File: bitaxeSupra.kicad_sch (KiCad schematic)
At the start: 20 parts, among them J1 PJ-036AH-SMT

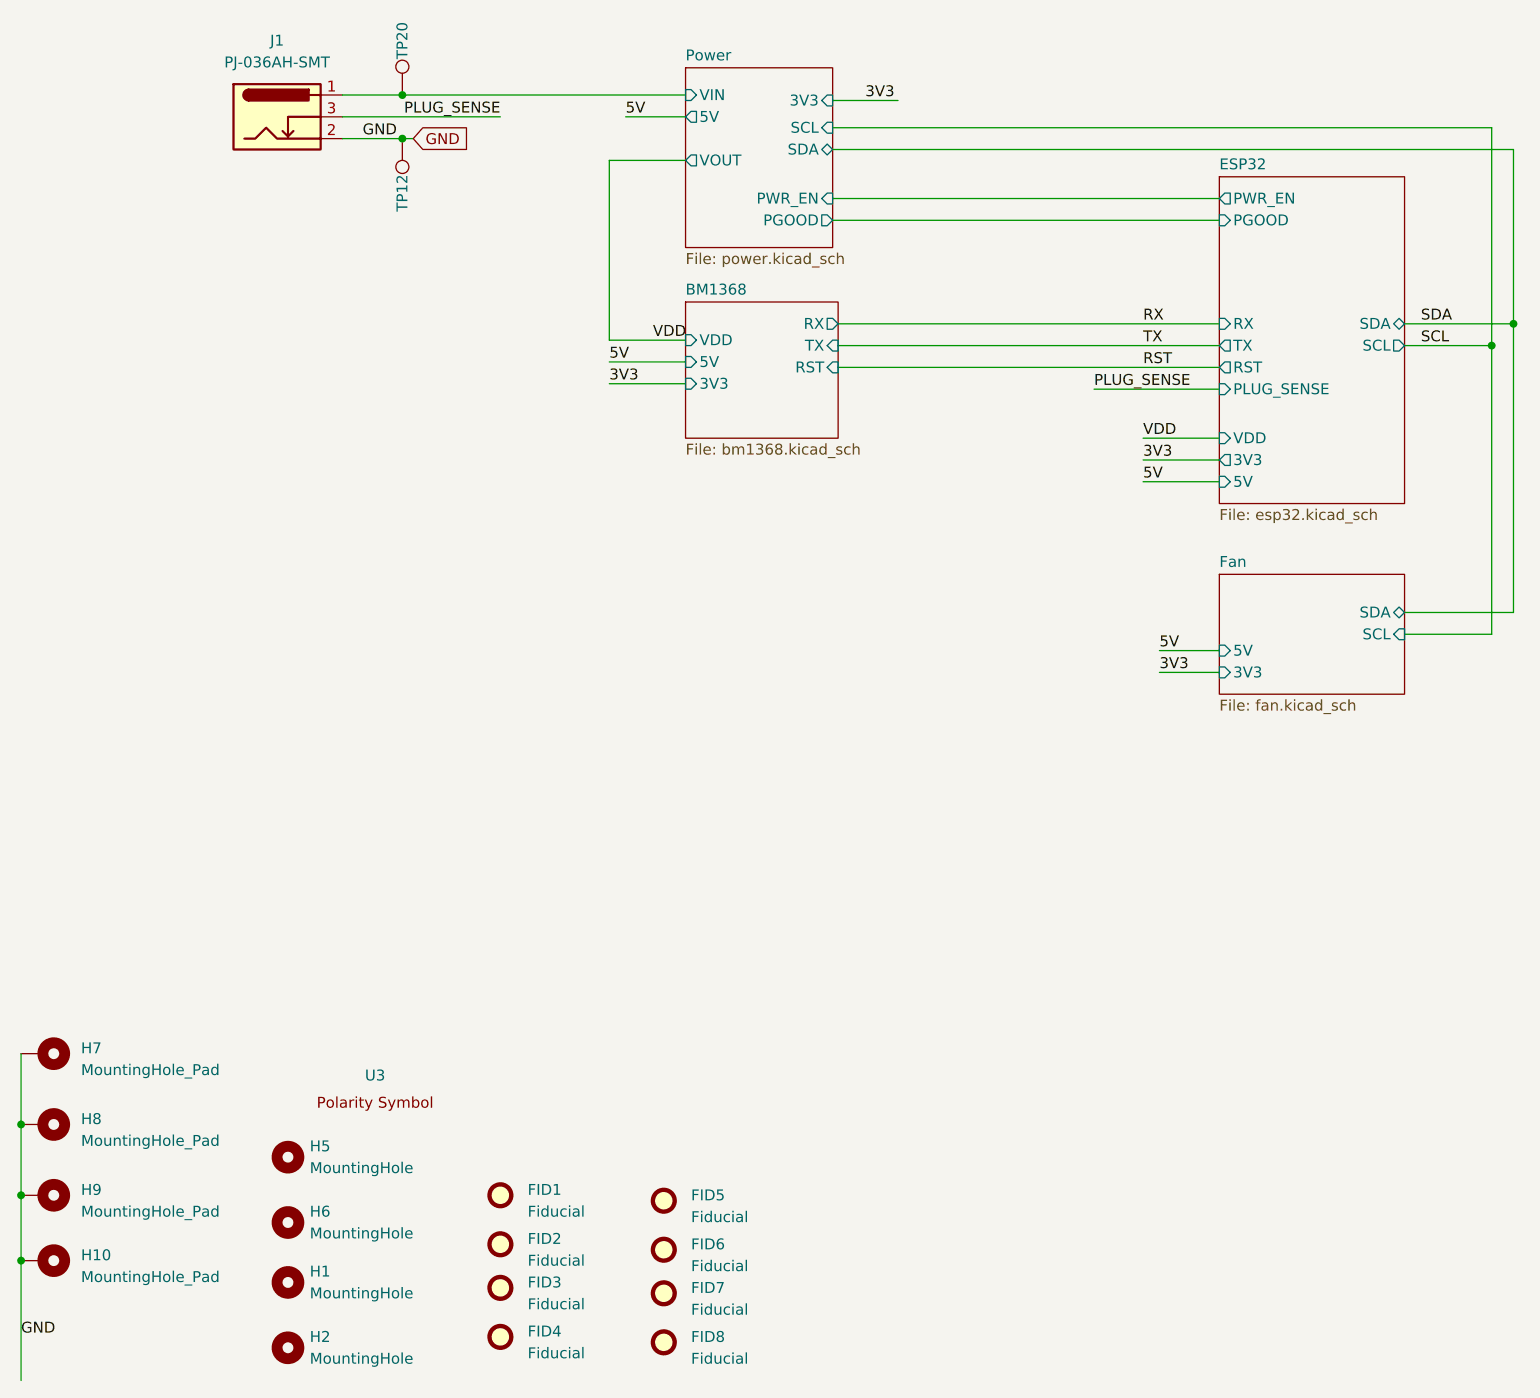
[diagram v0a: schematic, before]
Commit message: hooked up TEMP_P and TEMP_N. bumped version everywhere to 402
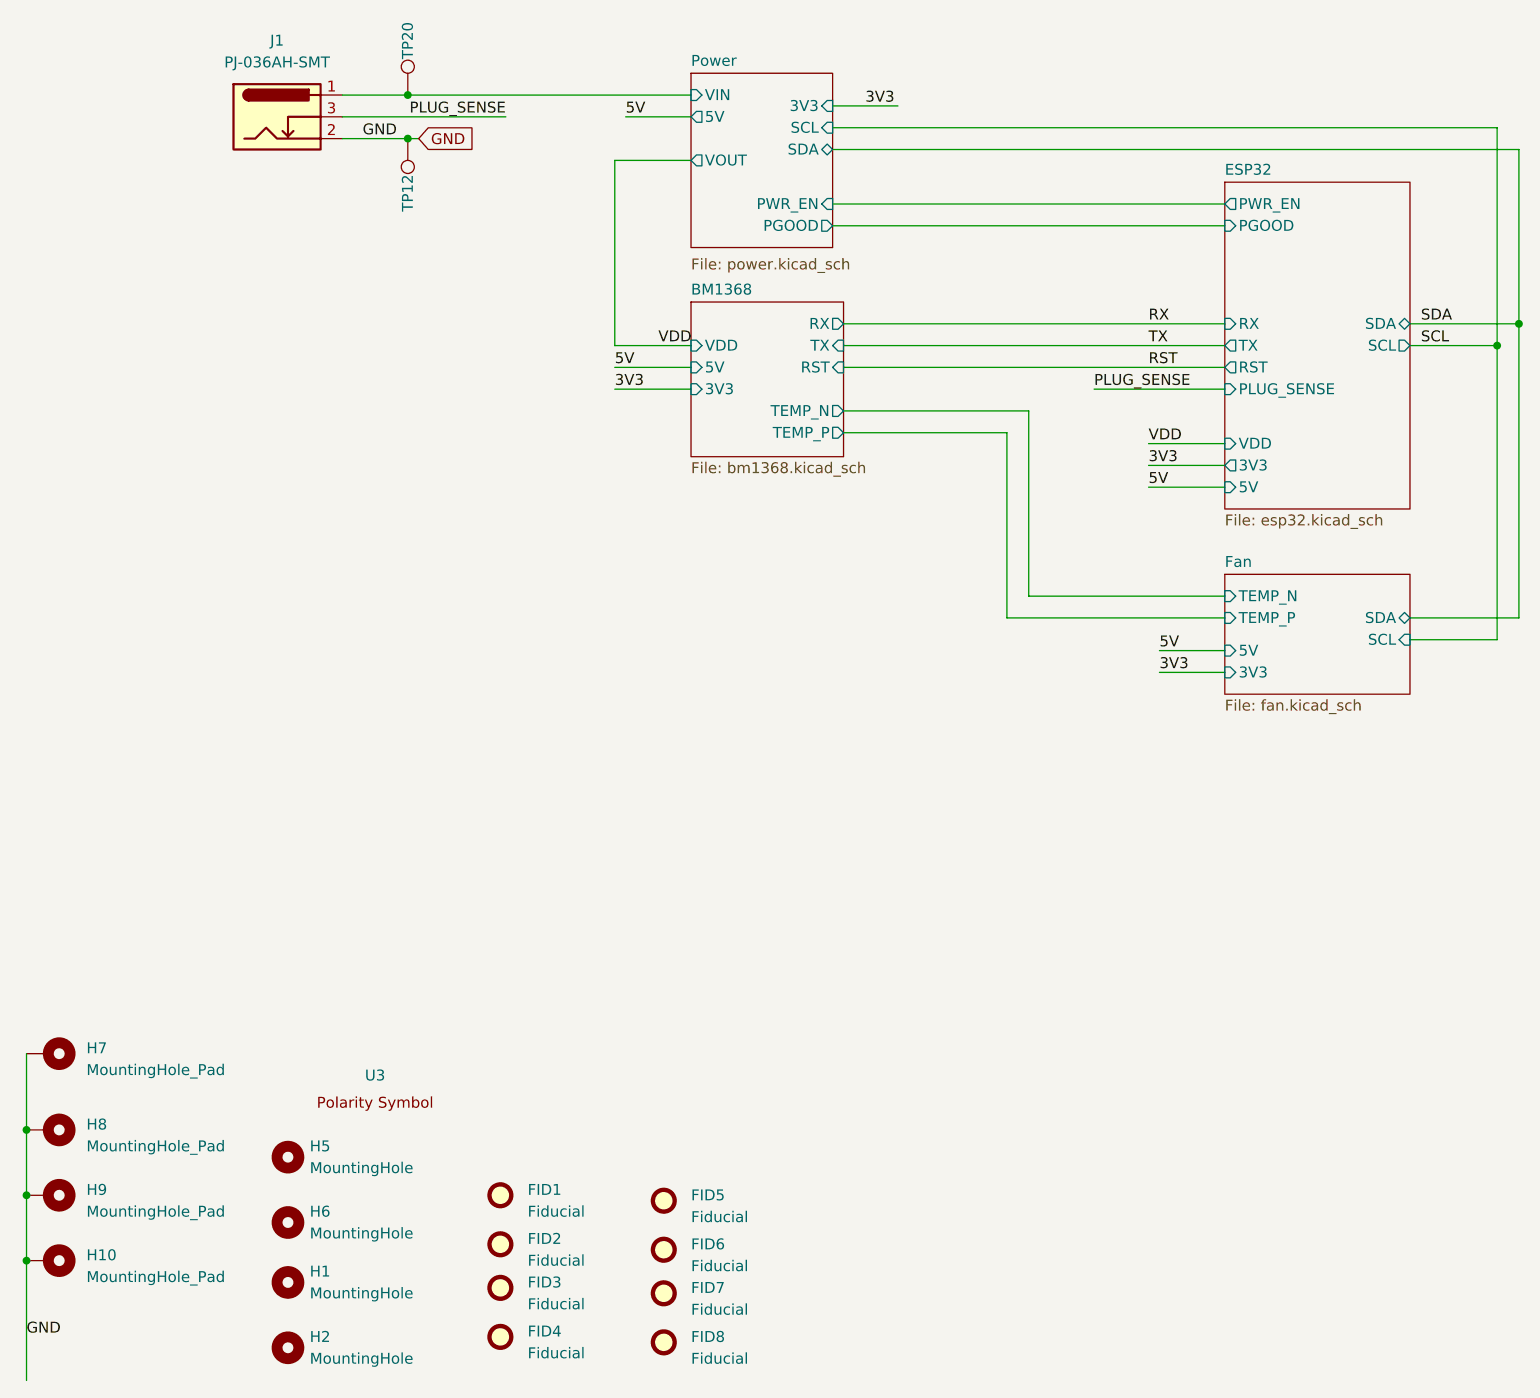
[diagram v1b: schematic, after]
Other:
- sheet BM1368 ports: added TEMP_N, TEMP_P; removed none
- sheet Fan ports: added TEMP_N, TEMP_P; removed none
- moved on the sheet: H10, H7, H8, H9, TP12, TP20

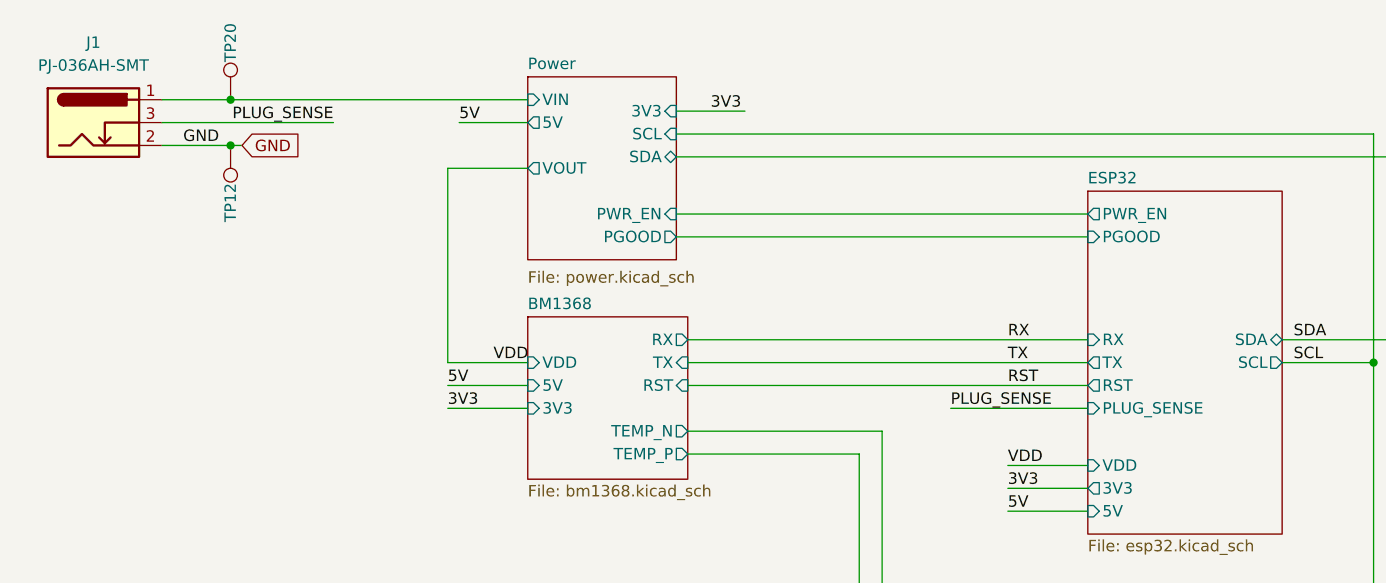
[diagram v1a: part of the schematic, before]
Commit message: changed fan capacitor to 100uF ceramic. Switched level shifter to SN74AVC4T774 for #146
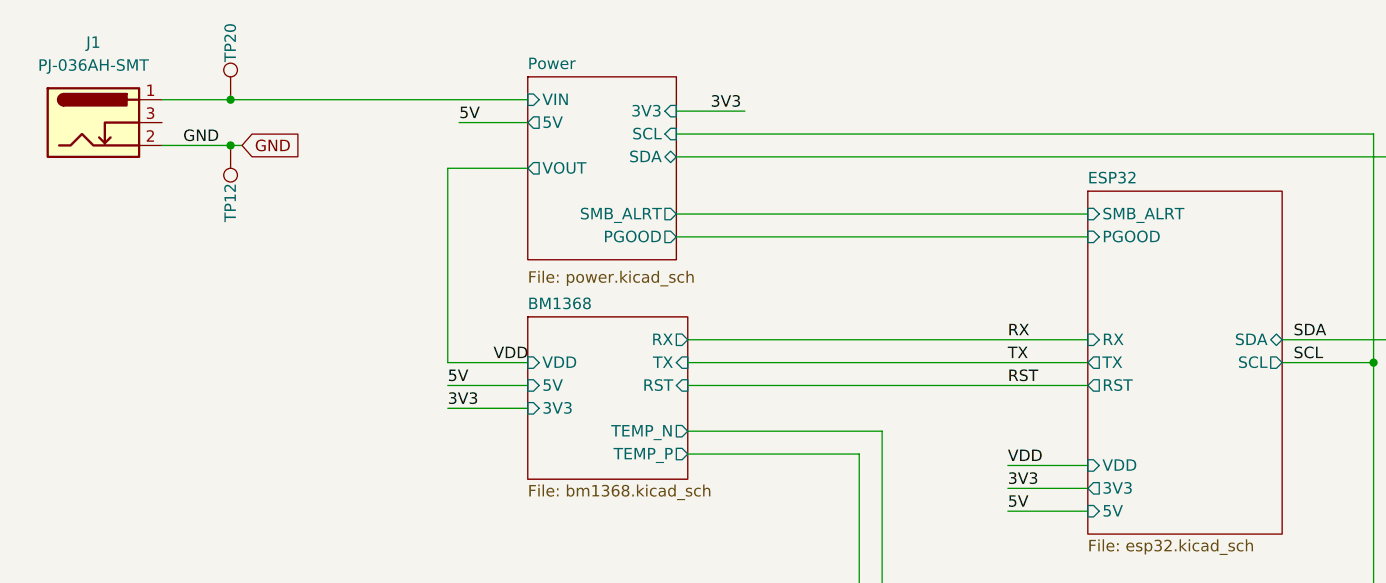
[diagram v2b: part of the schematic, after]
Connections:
- net PLUG_SENSE: no longer names the net of J1.3
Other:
- sheet ESP32 ports: added SMB_ALRT; removed PLUG_SENSE, PWR_EN
- sheet Power ports: added SMB_ALRT; removed PWR_EN
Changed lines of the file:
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@@
-	(wire
-		(pts
-			(xy 160.02 77.47) (xy 175.26 77.47)
-		)
-		(stroke
-			(width 0)
-			(type default)
-		)
-	)
 	(wire
 		(pts
@@
 	(wire
 		(pts
-			(xy 72.39 45.72) (xy 91.44 45.72)
-		)
-		(stroke
-			(width 0)
-			(type default)
-		)
-	)
-	(wire
-		(pts
 			(xy 166.37 83.82) (xy 175.26 83.82)
 		)
@@
 	(wire
 		(pts
+			(xy 196.85 69.85) (xy 209.55 69.85)
+		)
+		(stroke
+			(width 0)
+			(type default)
+		)
+	)
+	(wire
+		(pts
+			(xy 35.56 163.83) (xy 35.56 171.45)
+		)
+		(stroke
+			(width 0)
+			(type default)
+		)
+	)
+	(wire
+		(pts
+			(xy 104.14 77.47) (xy 113.03 77.47)
+		)
+		(stroke
+			(width 0)
+			(type default)
+		)
+	)
+	(wire
+		(pts
+			(xy 130.81 69.85) (xy 175.26 69.85)
+		)
+		(stroke
+			(width 0)
+			(type default)
+		)
+	)
+	(wire
+		(pts
+			(xy 196.85 104.14) (xy 209.55 104.14)
+		)
+		(stroke
+			(width 0)
+			(type default)
+		)
+	)
+	(wire
+		(pts
+			(xy 104.14 72.39) (xy 104.14 50.8)
+		)
+		(stroke
+			(width 0)
+			(type default)
+		)
+	)
+	(wire
+		(pts
+			(xy 130.81 80.01) (xy 152.4 80.01)
+		)
+		(stroke
+			(width 0)
+			(type default)
+		)
+	)
+	(wire
+		(pts
+			(xy 196.85 106.68) (xy 207.01 106.68)
+		)
+		(stroke
+			(width 0)
+			(type default)
+		)
+	)
+	(wire
+		(pts
+			(xy 104.14 74.93) (xy 113.03 74.93)
+		)
+		(stroke
+			(width 0)
+			(type default)
+		)
+	)
+	(wire
+		(pts
+			(xy 149.86 82.55) (xy 130.81 82.55)
+		)
+		(stroke
+			(width 0)
+			(type default)
+		)
+	)
+	(wire
+		(pts
+			(xy 209.55 104.14) (xy 209.55 69.85)
+		)
+		(stroke
+			(width 0)
+			(type default)
+		)
+	)
+	(wire
+		(pts
+			(xy 129.54 58.42) (xy 175.26 58.42)
+		)
+		(stroke
+			(width 0)
+			(type default)
+		)
+	)
+	(wire
+		(pts
+			(xy 167.64 107.95) (xy 175.26 107.95)
+		)
+		(stroke
+			(width 0)
+			(type default)
+		)
+	)
+	(wire
+		(pts
 			(xy 129.54 55.88) (xy 175.26 55.88)
 		)
@@
 	(wire
 		(pts
-			(xy 196.85 69.85) (xy 209.55 69.85)
-		)
-		(stroke
-			(width 0)
-			(type default)
-		)
-	)
-	(wire
-		(pts
-			(xy 35.56 163.83) (xy 35.56 171.45)
-		)
-		(stroke
-			(width 0)
-			(type default)
-		)
-	)
-	(wire
-		(pts
-			(xy 104.14 77.47) (xy 113.03 77.47)
-		)
-		(stroke
-			(width 0)
-			(type default)
-		)
-	)
-	(wire
-		(pts
-			(xy 130.81 69.85) (xy 175.26 69.85)
-		)
-		(stroke
-			(width 0)
-			(type default)
-		)
-	)
-	(wire
-		(pts
-			(xy 196.85 104.14) (xy 209.55 104.14)
-		)
-		(stroke
-			(width 0)
-			(type default)
-		)
-	)
-	(wire
-		(pts
-			(xy 104.14 72.39) (xy 104.14 50.8)
-		)
-		(stroke
-			(width 0)
-			(type default)
-		)
-	)
-	(wire
-		(pts
-			(xy 130.81 80.01) (xy 152.4 80.01)
-		)
-		(stroke
-			(width 0)
-			(type default)
-		)
-	)
-	(wire
-		(pts
-			(xy 196.85 106.68) (xy 207.01 106.68)
-		)
-		(stroke
-			(width 0)
-			(type default)
-		)
-	)
-	(wire
-		(pts
-			(xy 104.14 74.93) (xy 113.03 74.93)
-		)
-		(stroke
-			(width 0)
-			(type default)
-		)
-	)
-	(wire
-		(pts
-			(xy 149.86 82.55) (xy 130.81 82.55)
-		)
-		(stroke
-			(width 0)
-			(type default)
-		)
-	)
-	(wire
-		(pts
-			(xy 209.55 104.14) (xy 209.55 69.85)
-		)
-		(stroke
-			(width 0)
-			(type default)
-		)
-	)
-	(wire
-		(pts
-			(xy 129.54 58.42) (xy 175.26 58.42)
-		)
-		(stroke
-			(width 0)
-			(type default)
-		)
-	)
-	(wire
-		(pts
-			(xy 167.64 107.95) (xy 175.26 107.95)
-		)
-		(stroke
-			(width 0)
-			(type default)
-		)
-	)
-	(wire
-		(pts
 			(xy 35.56 179.07) (xy 35.56 193.04)
 		)
@@
 		)
 	)
-	(label "PLUG_SENSE"
-		(at 91.44 45.72 180)
+	(label "VDD"
+		(at 166.37 83.82 0)
 		(fields_autoplaced yes)
 		(effects
@@
 				(size 1.27 1.27)
 			)
-			(justify right bottom)
-		)
-	)
-	(label "VDD"
-		(at 166.37 83.82 0)
+			(justify left bottom)
+		)
+	)
+	(label "3V3"
+		(at 104.14 77.47 0)
 		(fields_autoplaced yes)
 		(effects
@@
 		)
 	)
-	(label "3V3"
-		(at 104.14 77.47 0)
+	(label "RST"
+		(at 166.37 74.93 0)
 		(fields_autoplaced yes)
 		(effects
@@
 		)
 	)
-	(label "RST"
-		(at 166.37 74.93 0)
+	(label "VDD"
+		(at 109.22 72.39 0)
 		(fields_autoplaced yes)
 		(effects
@@
 		)
 	)
-	(label "VDD"
-		(at 109.22 72.39 0)
+	(label "5V"
+		(at 105.41 45.72 0)
 		(fields_autoplaced yes)
 		(effects
@@
 	)
 	(label "5V"
-		(at 105.41 45.72 0)
+		(at 167.64 107.95 0)
 		(fields_autoplaced yes)
 		(effects
@@
 		)
 	)
-	(label "5V"
-		(at 167.64 107.95 0)
+	(label "SDA"
+		(at 198.12 69.85 0)
 		(fields_autoplaced yes)
 		(effects
@@
 		)
 	)
-	(label "SDA"
-		(at 198.12 69.85 0)
+	(label "GND"
+		(at 35.56 187.96 0)
 		(fields_autoplaced yes)
 		(effects
@@
 		)
 	)
-	(label "GND"
-		(at 35.56 187.96 0)
+	(label "RX"
+		(at 166.37 69.85 0)
 		(fields_autoplaced yes)
 		(effects
@@
 		)
 	)
-	(label "RX"
-		(at 166.37 69.85 0)
+	(label "3V3"
+		(at 133.35 44.45 0)
 		(fields_autoplaced yes)
 		(effects
@@
 	)
 	(label "3V3"
-		(at 133.35 44.45 0)
+		(at 166.37 86.36 0)
 		(fields_autoplaced yes)
 		(effects
@@
 		)
 	)
-	(label "3V3"
-		(at 166.37 86.36 0)
+	(label "SCL"
+		(at 198.12 72.39 0)
 		(fields_autoplaced yes)
 		(effects
@@
 		)
 	)
-	(label "SCL"
-		(at 198.12 72.39 0)
+	(label "5V"
+		(at 166.37 88.9 0)
 		(fields_autoplaced yes)
 		(effects
@@
 		)
 	)
-	(label "5V"
-		(at 166.37 88.9 0)
+	(label "3V3"
+		(at 167.64 110.49 0)
 		(fields_autoplaced yes)
 		(effects
@@
 		)
 	)
-	(label "3V3"
-		(at 167.64 110.49 0)
+	(label "5V"
+		(at 104.14 74.93 0)
 		(fields_autoplaced yes)
 		(effects
@@
 		)
 	)
-	(label "5V"
-		(at 104.14 74.93 0)
+	(label "GND"
+		(at 78.74 48.26 180)
 		(fields_autoplaced yes)
 		(effects
@@
 				(size 1.27 1.27)
 			)
-			(justify left bottom)
-		)
-	)
-	(label "GND"
-		(at 78.74 48.26 180)
-		(fields_autoplaced yes)
-		(effects
-			(font
-				(size 1.27 1.27)
-			)
 			(justify right bottom)
-		)
-	)
-	(label "PLUG_SENSE"
-		(at 160.02 77.47 0)
-		(fields_autoplaced yes)
-		(effects
-			(font
-				(size 1.27 1.27)
-			)
-			(justify left bottom)
 		)
 	)
@@
 			)
 		)
-		(pin "PWR_EN" input
+		(pin "SMB_ALRT" output
 			(at 129.54 55.88 0)
 			(effects
@@
 			)
 		)
-		(pin "PWR_EN" output
+		(pin "SMB_ALRT" input
 			(at 175.26 55.88 180)
 			(effects
 				(font
-					(size 1.27 1.27)
-				)
-				(justify left)
-			)
-		)
-		(pin "PLUG_SENSE" input
-			(at 175.26 77.47 180)
-			(effects
-				(font

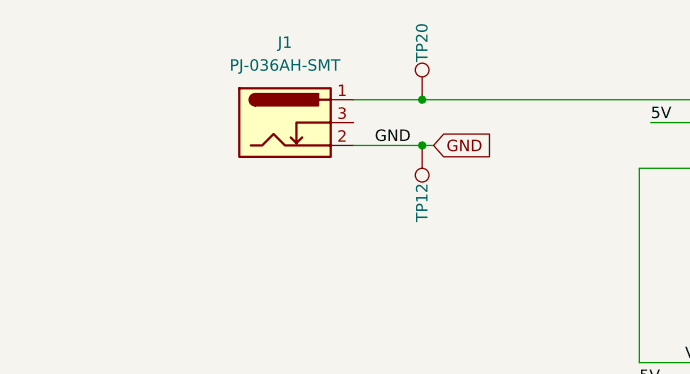
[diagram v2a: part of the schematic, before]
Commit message: changed barrel plug to 54-00164 for #158
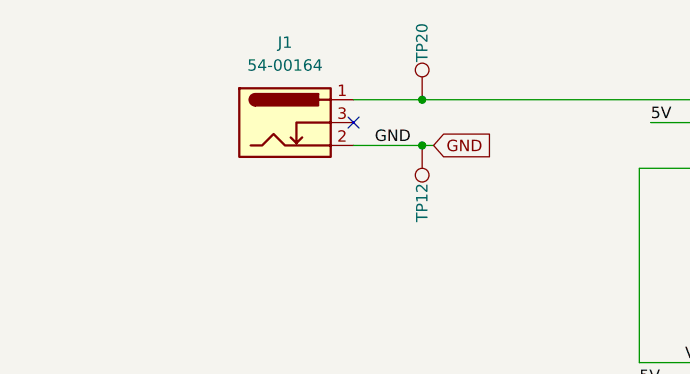
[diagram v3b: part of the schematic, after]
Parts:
- J1: value PJ-036AH-SMT -> 54-00164; footprint Connector_BarrelJack:BarrelJack_CUI_PJ-036AH-SMT_Horizontal -> bitaxe:TENSILITY_54-00164; DK CP-036AHPJTR-ND -> 839-54-00164CT-ND; LCSC (none) -> C431534; PARTNO PJ-036AH-SMT -> 54-00164
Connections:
- no-connect marks 0 -> 1
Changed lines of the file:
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@@
 		(color 0 0 0 0)
+	)
+	(no_connect
+		(at 72.39 45.72)
 	)
 	(wire
@@
 			)
 		)
-		(property "Value" "PJ-036AH-SMT"
+		(property "Value" "54-00164"
 			(at 64.77 39.37 0)
 			(effects
@@
 			)
 		)
-		(property "Footprint" "Connector_BarrelJack:BarrelJack_CUI_PJ-036AH-SMT_Horizontal"
+		(property "Footprint" "bitaxe:TENSILITY_54-00164"
 			(at 66.04 46.736 0)
 			(effects
@@
 			)
 		)
-		(property "Datasheet" "https://www.cuidevices.com/product/resource/pj-036ah-smt-tr.pdf"
+		(property "Datasheet" "https://tensility.s3.amazonaws.com/uploads/pdffiles/54-00164.pdf?X-Amz-Expires=600&X-Amz-Date=20240425T233931Z&X-Amz-Algorithm=AWS4-HMAC-SHA256&X-Amz-Credential=AKIAIS2S4WRDQDSWDRZQ%2F20240425%2Fus-west-2%2Fs3%2Faws4_request&X-Amz-SignedHeaders=host&X-Amz-Signature=db47604833b748f16eb1b48a1cb56220ad6cd713e88f354ff5cc2bea6dae9c43"
 			(at 66.04 46.736 0)
 			(effects
@@
 			)
 		)
-		(property "DK" "CP-036AHPJTR-ND"
+		(property "DK" "839-54-00164CT-ND"
 			(at 64.77 45.72 0)
 			(effects
@@
 			)
 		)
-		(property "PARTNO" "PJ-036AH-SMT"
+		(property "PARTNO" "54-00164"
 			(at 64.77 45.72 0)
 			(effects
+				(font
+					(size 1.27 1.27)
+				)
+				(hide yes)
+			)
+		)
+		(property "LCSC" "C431534"
+			(at 64.77 45.72 0)
+			(effects
